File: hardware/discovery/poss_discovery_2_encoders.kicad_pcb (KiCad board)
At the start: 2 copper layers, 96.5 x 66 mm, 110 parts, among them CON1 USB-MICRO-B, SW1 SW_PUSH, SW10 SW_PUSH, SW11 SW_PUSH, SW12 SW_PUSH, SW13 SW_PUSH, SW14 SW_PUSH, SW15 SW_PUSH, SW16 SW_PUSH, SW18 SW_PUSH, SW19 SW_PUSH, SW2 SW_PUSH, SW20 SW_PUSH, SW21 SW_PUSH, SW22 SW_PUSH, SW3 SW_PUSH, SW4 SW_PUSH, SW5 SW_PUSH, SW6 SW_PUSH, SW7 SW_PUSH, SW8 SW_PUSH, SW9 SW_PUSH, U2 MCP73831, U3 BD33IA5, U4 STM32F407VG, U5 SGTL5000, U6 encoder_and_switch, U7 encoder_and_switch, U8 MOLEX_microSD_47219-2001, U9 SSD1306, X1 CRYSTAL

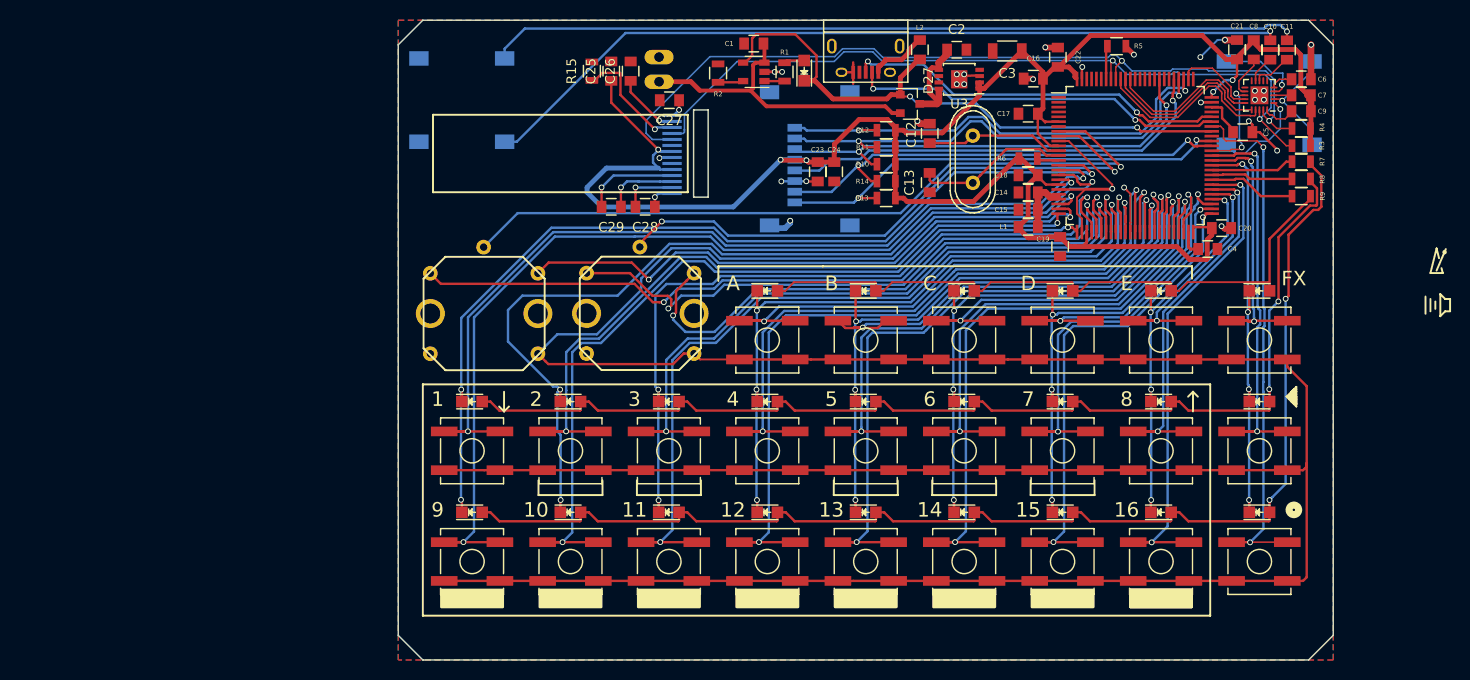
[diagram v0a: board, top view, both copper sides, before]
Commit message: Discovery: Add two encoders and remove the BPM button
BPM and volume will be changed with a long press of the play button and
the encoders
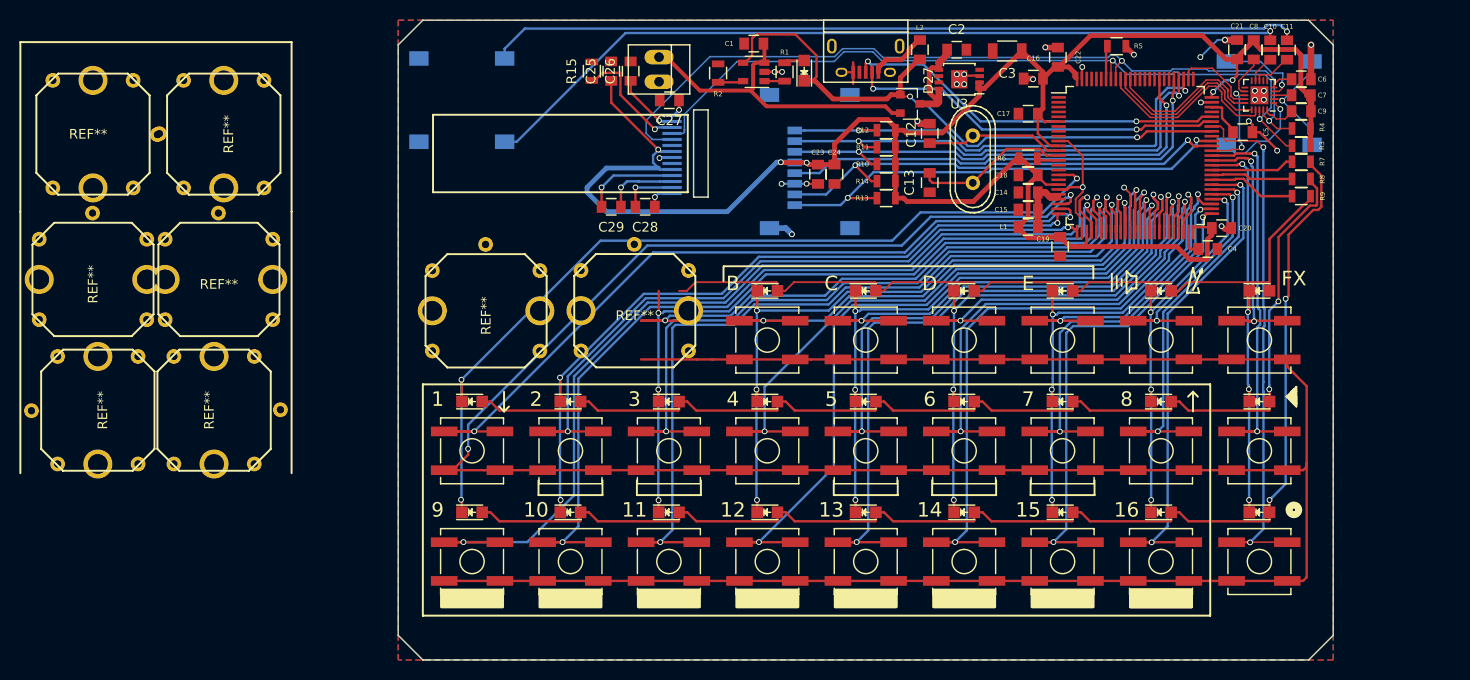
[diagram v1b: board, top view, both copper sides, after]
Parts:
- removed U6, U7: encoder_and_switch, stm32f4-disco:encoder_EC12D
- added REF**: encoder_EC12D, stm32f4-disco:encoder_EC12D, F.Cu at (89.1, 108.7)
- added REF**: encoder_EC12D, stm32f4-disco:encoder_EC12D, F.Cu at (104.4, 108.7)
- added REF**: encoder_EC12D, stm32f4-disco:encoder_EC12D, F.Cu at (48.5, 90.5)
- added REF**: encoder_EC12D, stm32f4-disco:encoder_EC12D, F.Cu at (62.0, 90.5)
- added REF**: encoder_EC12D, stm32f4-disco:encoder_EC12D, F.Cu at (61.5, 105.5)
- added REF**: encoder_EC12D, stm32f4-disco:encoder_EC12D, F.Cu at (48.5, 105.5)
- added REF**: encoder_EC12D, stm32f4-disco:encoder_EC12D, F.Cu at (49.0, 119.0)
- added REF**: encoder_EC12D, stm32f4-disco:encoder_EC12D, F.Cu at (61.0, 119.0)
- BT1: moved to F.Cu
- moved ? 25.2 mm to (162.1, 103.4)
- moved U8 0.28 mm to (118.3, 100.2)
- moved C23 0.26 mm to (123.3, 94.6)
- moved C24 0.26 mm to (125.0, 94.6)
- turned BT1 to 270 degrees
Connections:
- SW18 pad 1: BA -> BB
- SW19 pad 1: BB -> BC
- SW20 pad 1: BC -> BD
- SW21 pad 1: BD -> BE
- SW22 pad 1: BE -> BPM_VOL
- U4 pad 15: COL1 -> Net-(U4-Pad15)
- U4 pad 16: B1 -> Net-(U4-Pad16)
- U4 pad 17: COL2 -> COL1
- U4 pad 18: B9 -> Net-(U4-Pad18)
- U4 pad 24: ENC_1_B -> B1
- U4 pad 25: B2 -> COL2
- U4 pad 26: B10 -> B2
- U4 pad 29: COL3 -> B9
- U4 pad 30: ENC_1_A -> B10
- U4 pad 31: ENC_2_A -> COL3
- U4 pad 32: ENC_2_B -> BA
- U4 pad 36: BA -> BB
- U4 pad 41: BB -> BC
- U4 pad 45: BC -> BD
- U4 pad 53: BD -> BE
- U4 pad 55: BE -> BPM_VOL
- U4 pad 8: ENC_1_SW -> Net-(U4-Pad8)
- U4 pad 9: ENC_2_SW -> Net-(U4-Pad9)
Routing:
- net ENC_1_A: track 77.9 -> 0.00 mm, vias 2 -> 0
- net ENC_1_SW: track 77.4 -> 0.00 mm, vias 1 -> 0
- net ENC_2_A: track 66.1 -> 0.00 mm, vias 2 -> 0
- net ENC_1_B: track 61.9 -> 0.00 mm, vias 2 -> 0
- net ENC_2_SW: track 61.3 -> 0.00 mm, vias 2 -> 0
- net ENC_2_B: track 60.6 -> 0.00 mm, vias 2 -> 0
- net BPM_VOL: track 0.00 -> 26.3 mm, vias 0 -> 2
- net COL2: track 95.8 -> 75.4 mm
- net B1: track 93.9 -> 81.7 mm
- net Net-(D19-Pad2): track 68.5 -> 79.8 mm
- net BB: track 46.8 -> 56.6 mm
- net COL1: track 97.8 -> 90.2 mm
- net BD: track 33.2 -> 40.6 mm
- net GND: track 61.7 -> 54.7 mm
- net BC: track 40.6 -> 47.5 mm
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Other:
- board text removed: "A"
